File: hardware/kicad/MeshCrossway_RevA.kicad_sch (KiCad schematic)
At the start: 39 parts, among them J1 Waveshare ESP32-S3-Touch-LCD-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, J2 HOST DEBUG, U1 LOCAL 5V SOURCE — TBD, U2 XIAO + Wio-SX1262, U3 XIAO + Wio-SX1262, U4 Uputronics MAX-M10S 3V

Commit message: Use full mechanical GNSS module footprint
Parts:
- U4: footprint Connector_PinSocket_2.54mm:PinSocket_1x07_P2.54mm_Vertical -> MeshCrossway:Module_Uputronics_MAX_M10S_3V_MECH_APPROX
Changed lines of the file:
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@@
 			)
 		)
-		(property "Footprint" "Connector_PinSocket_2.54mm:PinSocket_1x07_P2.54mm_Vertical"
+		(property "Footprint" "MeshCrossway:Module_Uputronics_MAX_M10S_3V_MECH_APPROX"
 			(at 57.15 132.08 0)
 			(hide yes)

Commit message: Add JST-PH 2.0 battery input connector to schematic
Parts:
- added J5: BATTERY JST-PH 2.0, Connector_JST:JST_PH_B2B-PH-K_1x02_P2.00mm_Vertical, symbol MeshCrossway:BATTERY_JST_PH2
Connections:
- net BAT: now also J5.1 (BAT+)
- net GND: now also J5.2 (GND)
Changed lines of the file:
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@@
+	)
+	(symbol
+		(lib_id "MeshCrossway:BATTERY_JST_PH2")
+		(at 14.59 88.9 0)
+		(unit 1)
+		(body_style 1)
+		(exclude_from_sim no)
+		(in_bom yes)
+		(on_board yes)
+		(in_pos_files yes)
+		(dnp no)
+		(property "Reference" "J5"
+			(at 14.59 81.28 0)
+			(show_name no)
+			(do_not_autoplace no)
+			(effects (font (size 1 1) (bold yes)))
+		)
+		(property "Value" "BATTERY JST-PH 2.0"
+			(at 14.59 78.74 0)
+			(show_name no)
+			(do_not_autoplace no)
+			(effects (font (size 0.86 0.86)))
+		)
+		(property "Footprint" "Connector_JST:JST_PH_B2B-PH-K_1x02_P2.00mm_Vertical"
+			(at 14.59 88.9 0)
+			(hide yes)
+			(show_name no)
+			(do_not_autoplace no)
+			(effects (font (size 1 1)))
+		)
+		(property "Datasheet" ""
+			(at 14.59 88.9 0)
+			(hide yes)
+			(show_name no)
+			(do_not_autoplace no)
+			(effects (font (size 1 1)))
+		)
+		(property "Description" "Battery input: 2-pin JST-PH 2.0 mm; pin 1 BAT+, pin 2 GND. Verify mating battery polarity before assembly."
+			(at 14.59 88.9 0)
+			(hide yes)
+			(show_name no)
+			(do_not_autoplace no)
+			(effects (font (size 1 1)))
+		)
+		(pin "1"
+		)
+		(pin "2"
+		)
+		(instances
+			(project "MeshCrossway_v1"
+				(path "/625b3c66-94c9-41de-b2bc-9cf686ed83a7"
+					(reference "J5")
+					(unit 1)
+				)
+			)
+		)
 	)
 	(symbol

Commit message: Update Rev A KiCad PCB schematic and validated footprints
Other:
- moved on the sheet: J5, U1

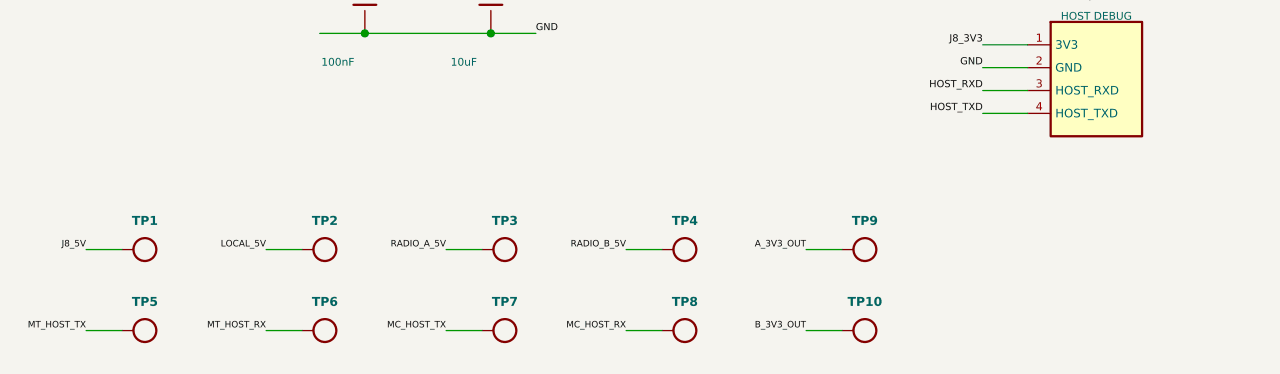
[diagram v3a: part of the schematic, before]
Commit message: Rework test points and PCB placement in KiCad RevA
Schematic: remove the UART test points (MC/MT_HOST_TX/RX, TP5-TP8) with their wires and labels. Rename and move the power test points to a single row: J85V, 5V, Ra5Vin, Rb5Vin, Ra3v3out, Rb3v3out. Reference designators are now descriptive instead of TPn.

PCB: sync to the schematic, with the renamed test points placed in a cluster near x=254-262, y=73-77. Reposition J1, J2, JP1, JP3, U4, the battery, and the decoupling caps and resistors on the back side. Rotate several parts, regroup the GNSS-related parts, and drop the stale KiLib_Generator properties.

Project: update the used_designators list.
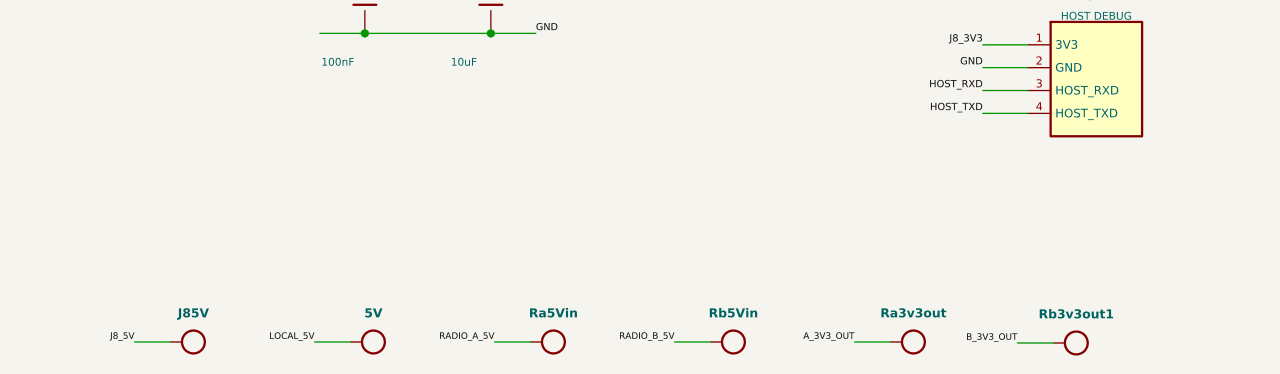
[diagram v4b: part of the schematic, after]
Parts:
- removed TP5, TP6, TP7, TP8: TestPoint, TestPoint:TestPoint_Pad_D2.0mm, symbol MeshCrossway:TP
- renumbered TP2 to 5V, TP1 to J85V, TP9 to Ra3v3out, TP3 to Ra5Vin, TP10 to Rb3v3out1, TP4 to Rb5Vin
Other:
- moved on the sheet: 5V, J85V, Ra3v3out, Ra5Vin, Rb3v3out1, Rb5Vin

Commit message: Restore and normalize TP1-TP10 test points
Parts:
- added TP5: MT_HOST_TX, TestPoint:TestPoint_Pad_D2.0mm, symbol MeshCrossway:TP
- added TP6: MT_HOST_RX, TestPoint:TestPoint_Pad_D2.0mm, symbol MeshCrossway:TP
- added TP7: MC_HOST_TX, TestPoint:TestPoint_Pad_D2.0mm, symbol MeshCrossway:TP
- added TP8: MC_HOST_RX, TestPoint:TestPoint_Pad_D2.0mm, symbol MeshCrossway:TP
- TP1: renamed from J85V; value TestPoint -> J8_5V
- TP10: renamed from Rb3v3out1; value TestPoint -> B_3V3_OUT
- TP2: renamed from 5V; value TestPoint -> LOCAL_5V
- TP3: renamed from Ra5Vin; value TestPoint -> RADIO_A_5V
- TP4: renamed from Rb5Vin; value TestPoint -> RADIO_B_5V
- TP9: renamed from Ra3v3out; value TestPoint -> A_3V3_OUT
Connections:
- net MC_HOST_RX: now also TP8.1 (TP)
- net MC_HOST_TX: now also TP7.1 (TP)
- net MT_HOST_RX: now also TP6.1 (TP)
- net MT_HOST_TX: now also TP5.1 (TP)

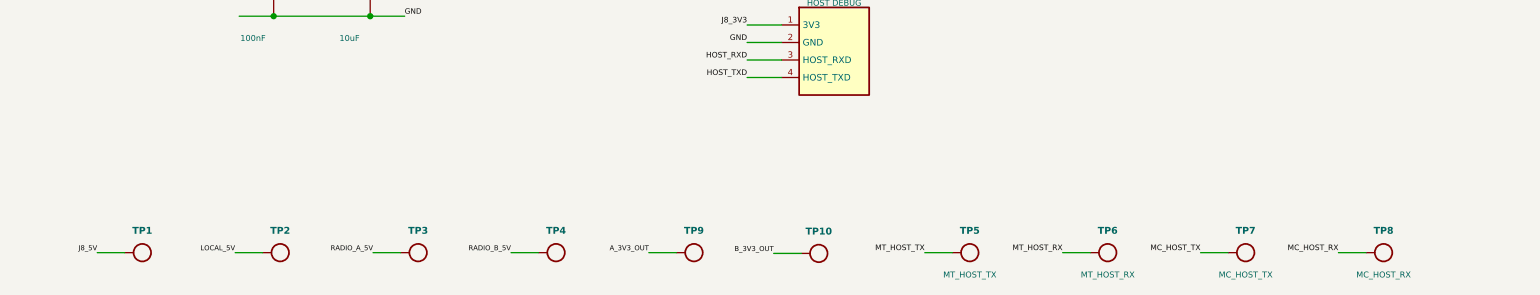
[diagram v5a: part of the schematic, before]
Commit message: Link PCB test points to schematic TP symbols
Replaced the old ad-hoc test point footprints (Ra3v3out1, Rb5Vin1, 5v1, etc.) in the PCB with TP1-TP10 footprints tied to the schematic symbols via their paths. The new footprints carry net-named values and are placed in a cluster at the board's lower-left. Added the missing symbol path on the MC_HOST_RX footprint and on one other footprint.

In the schematic, moved the 5V/3V3 test point row up and left and added MT/MC host TX/RX test points with their labels and wires. Reformatted the existing TP symbols to the standard KiCad layout. Cleared the stale used_designators list in the project file.
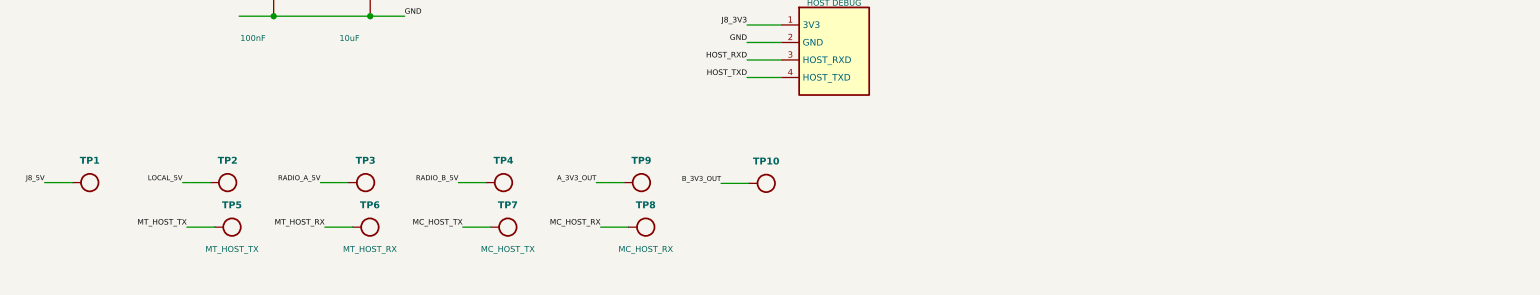
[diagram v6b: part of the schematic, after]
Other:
- moved on the sheet: TP1, TP10, TP2, TP3, TP4, TP5, TP6, TP7, TP8, TP9
